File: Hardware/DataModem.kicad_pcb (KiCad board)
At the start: 2 copper layers, 100 x 50 mm, 39 parts, among them J1 5V, J2 SERIAL, J3 DB9 FEMALE (DCE), J4 OUT, J5 IN, Q1 2N3904, U1 MAX232, U2 LM555, U3 LM555, U4 LM358

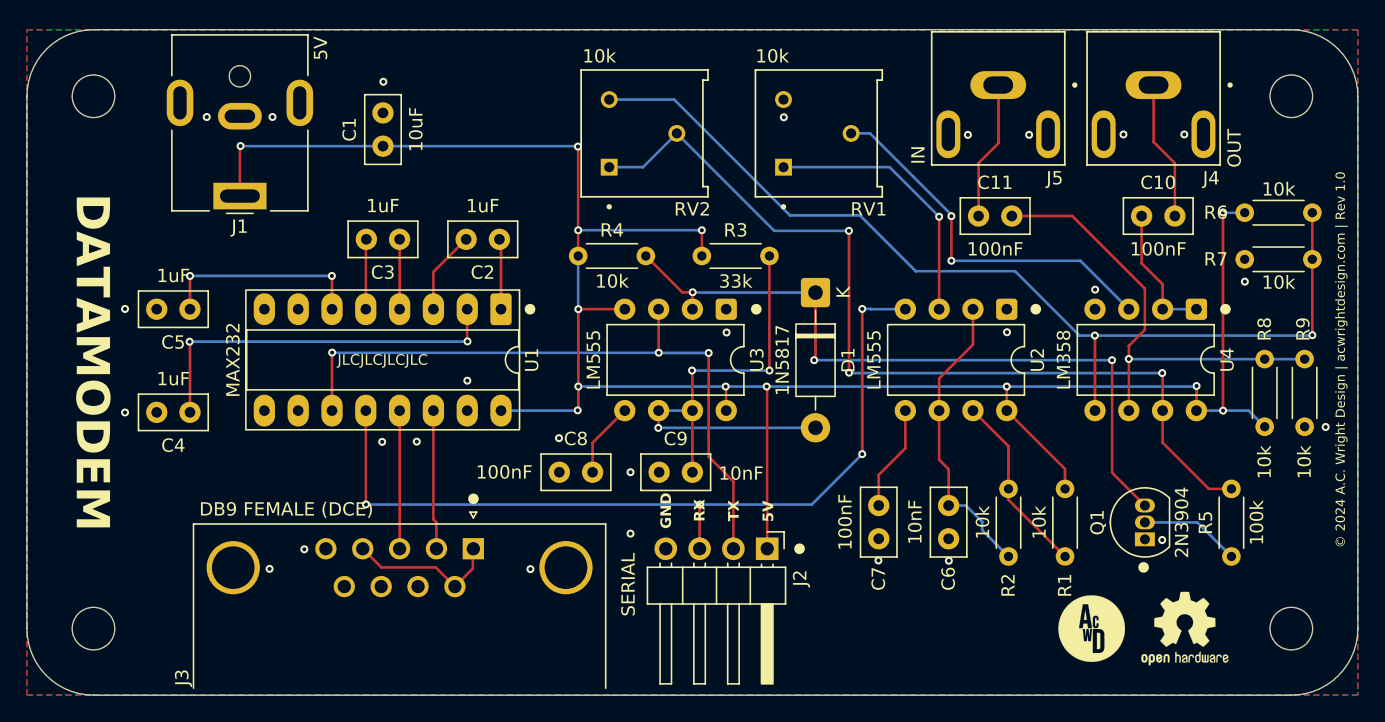
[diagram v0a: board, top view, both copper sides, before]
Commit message: Add screw terminal for power input
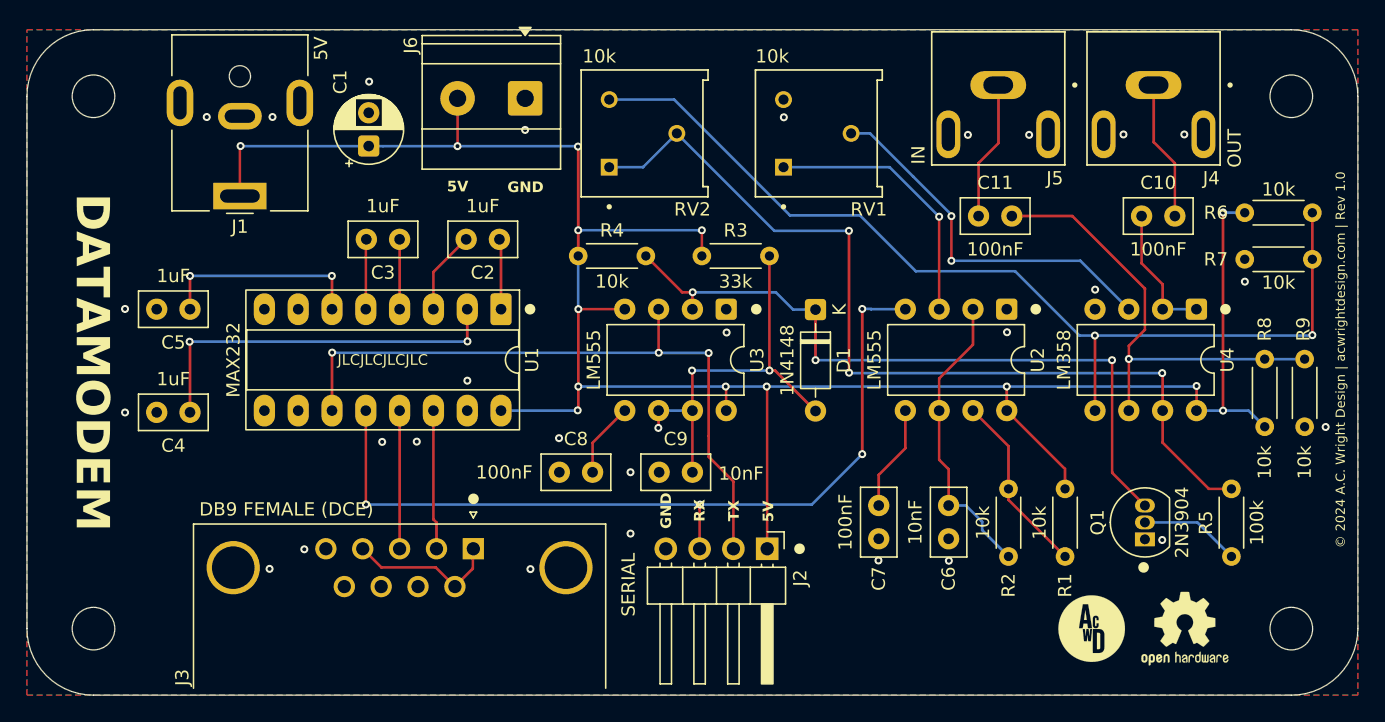
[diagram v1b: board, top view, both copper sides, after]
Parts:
- added J6: 5V, TerminalBlock_Phoenix:TerminalBlock_Phoenix_MKDS-1,5-2-5.08_1x02_P5.08mm_Horizontal, F.Cu at (117.4, 75.2)
- C1: footprint Capacitor_THT:C_Disc_D5.0mm_W2.5mm_P2.50mm -> Capacitor_THT:CP_Radial_D5.0mm_P2.50mm
- D1: value 1N5817 -> 1N4148; footprint Diode_THT:D_DO-41_SOD81_P10.16mm_Horizontal -> Diode_THT:D_DO-35_SOD27_P7.62mm_Horizontal
- moved D1 1.28 mm to (139.2, 91.0)
- moved C1 1.07 mm to (105.7, 78.7)
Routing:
- net Net-(D1-A): track 38.0 -> 30.9 mm
- net VCC: track 163.5 -> 167.1 mm, vias 13 -> 14
- net Net-(D1-K): track 54.6 -> 53.8 mm
- net GND: vias 27 -> 28

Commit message: Production fixes
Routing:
- net Net-(D1-A): track 30.9 -> 29.6 mm, vias 3 -> 2
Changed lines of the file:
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@@
-	)
-	(segment
-		(start 127.46 98.62)
-		(end 127.46 99.9)
-		(width 0.2)
-		(layer "F.Cu")
-		(net 12)
-	)
-	(segment
-		(start 127.46 99.9)
-		(end 127.44 99.92)
-		(width 0.2)
-		(layer "F.Cu")
-		(net 12)
 	)
 	(segment
@@
 		(size 0.6)
 		(drill 0.3)
-		(layers "F.Cu" "B.Cu")
-		(net 12)
-	)
-	(via
-		(at 127.44 99.92)
-		(size 0.6)
-		(drill 0.3)
